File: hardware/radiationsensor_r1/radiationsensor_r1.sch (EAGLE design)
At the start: 37 parts, among them CN1 1X06, U1 LMP7721, U2 MAX4477, U4 MAX4477, U5 50k

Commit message: radiation sensor r1 layout nearly complete
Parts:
- removed C17: 0.1uF, openct:CAP0603
- added C16: 1uF, openct:CAP0603
- added R16: THERM, openct:RESISTOR0603
- added R17: 10k, openct:RESISTOR0603
- C14: value 10uF 16V -> 10uF 10V
- C15: value 0.1uF -> 0.1uF 50V
- C4: value 1uF -> 1uF 50V
- CN1: value 1X06 -> 1X09; device openct:1X06 -> openct:1X09
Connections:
- removed net N$15: C14.1
- removed net VLOGIC: C17.1, CN1.1, U5.VDD
- new net VTEMP: CN1.1, R16.2, R17.1
- net 5V: now also C14.1, C16.1, CN1.8, R17.2, U5.VDD; no longer CN1.5
- net COMP_OUT: now also CN1.6; no longer CN1.3
- net CS: now also CN1.2
- net GND: now also C16.2, CN1.7, R16.1; no longer C17.2, CN1.4
- net MOSI: now also CN1.4
- net SCLK: now also CN1.3
- net VBIAS: now also CN1.9; no longer CN1.6
- net VOUT: now also CN1.5; no longer CN1.2
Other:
- moved on the sheet: C14, C15, C4

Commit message: schematic and board cleanup
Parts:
- C1: value 0.01uF -> 0.01uF 50V
- C6: value 0.1uF -> 4.7uF
- R10, R11, R8, R9: value 100k -> 51k
- R12: value 51.k -> 3.3k
- R3: value 10M -> 47M
- R5, R7: value 20k -> 33k
- renumbered D2 to D1
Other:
- note added: "(STACK OF 4"
- note added: "(~1100X GAIN)"
- note added: "(~15mv HYSTERESIS)"
- note added: "BASED ON MAXIM APPLICATION NOTE 2236"
- note added: "DECOUPLING"
- note added: "PETER JANSEN, JUNE 2015"
- note added: "PHOTODIODES)"
- note added: "RADIATION SENSOR (REVISION 1)"
- note added: "TEMPERATURE SENSOR"
- moved on the sheet: C10, C13, C14, C15, C16, R14, R15, R16, R17, R8, R9, U5

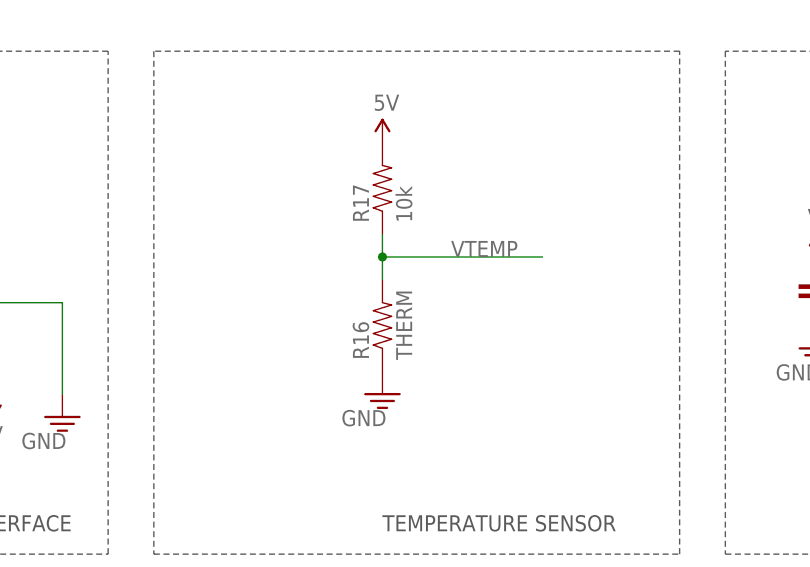
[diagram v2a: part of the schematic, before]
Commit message: Added part in library for radiation sensor rev1
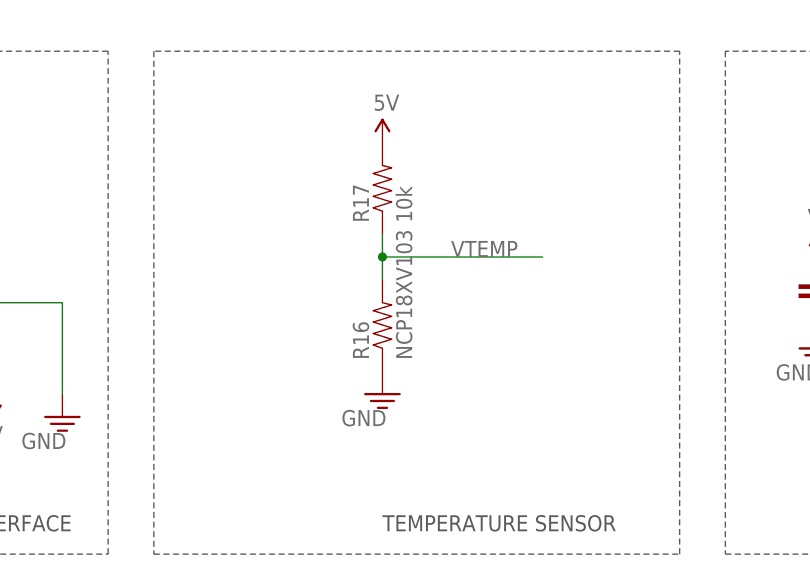
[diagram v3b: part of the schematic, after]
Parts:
- R16: value THERM -> NCP18XV103
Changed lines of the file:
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@@
 <part name="U$14" library="openct" deviceset="5V" device=""/>
 <part name="U$15" library="openct" deviceset="5V" device=""/>
-<part name="R16" library="openct" deviceset="RESISTOR" device="0603" value="THERM"/>
+<part name="R16" library="openct" deviceset="RESISTOR" device="0603" value="NCP18XV103"/>
 <part name="GND15" library="openct" deviceset="GND" device=""/>
 <part name="R17" library="openct" deviceset="RESISTOR" device="0603" value="10k"/>

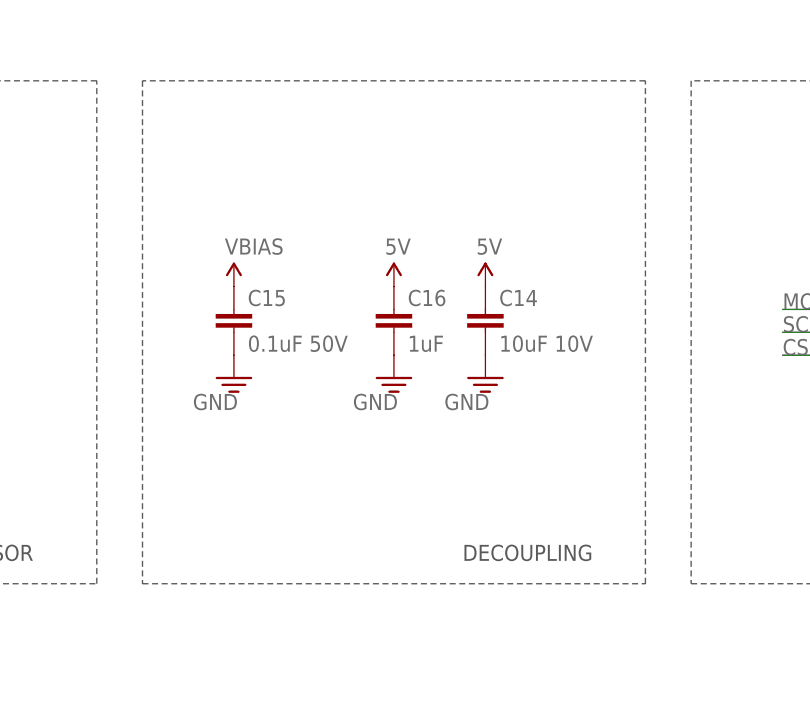
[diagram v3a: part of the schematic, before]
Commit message: Added shield connection to radiation sensor rev1
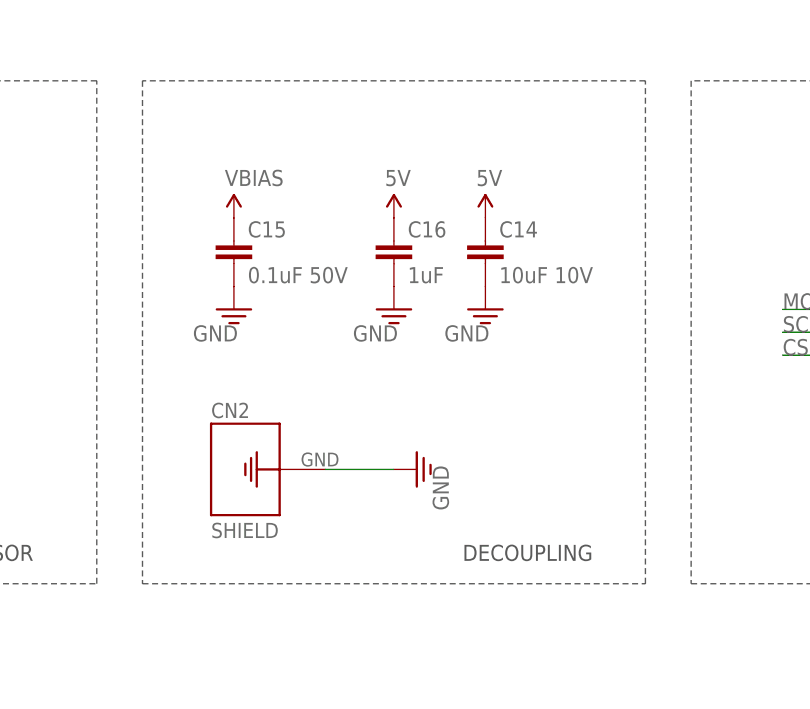
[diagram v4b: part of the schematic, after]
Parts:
- added CN2: GROUND-PAD, openct:GROUND-PAD
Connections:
- net GND: now also CN2.1
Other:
- moved on the sheet: C14, C15, C16
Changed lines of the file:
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@@
 <part name="U$6" library="openct" deviceset="5V" device=""/>
 <part name="GND16" library="openct" deviceset="GND" device=""/>
+<part name="CN2" library="openct" deviceset="GROUND-PAD" device=""/>
+<part name="GND18" library="openct" deviceset="GND" device=""/>
 </parts>
 <sheets>
@@
 <instance part="C13" gate="G$1" x="205.74" y="-66.04"/>
 <instance part="GND14" gate="1" x="205.74" y="-71.12"/>
-<instance part="C14" gate="G$1" x="119.38" y="-58.42"/>
-<instance part="GND19" gate="1" x="119.38" y="-63.5"/>
-<instance part="U$1" gate="G$1" x="91.44" y="-53.34"/>
-<instance part="C15" gate="G$1" x="91.44" y="-58.42"/>
-<instance part="GND20" gate="1" x="91.44" y="-63.5"/>
+<instance part="C14" gate="G$1" x="119.38" y="-50.8"/>
+<instance part="GND19" gate="1" x="119.38" y="-55.88"/>
+<instance part="U$1" gate="G$1" x="91.44" y="-45.72"/>
+<instance part="C15" gate="G$1" x="91.44" y="-50.8"/>
+<instance part="GND20" gate="1" x="91.44" y="-55.88"/>
 <instance part="D1" gate="G$1" x="-27.94" y="5.08" rot="R180"/>
 <instance part="U$14" gate="G$1" x="162.56" y="-48.26"/>
-<instance part="U$15" gate="G$1" x="119.38" y="-53.34"/>
+<instance part="U$15" gate="G$1" x="119.38" y="-45.72"/>
 <instance part="R16" gate="G$1" x="43.18" y="-60.96" rot="R90"/>
 <instance part="GND15" gate="1" x="43.18" y="-68.58"/>
@@
 <instance part="U$22" gate="G$1" x="0" y="-68.58" rot="R180"/>
 <instance part="U$23" gate="G$1" x="-7.62" y="-68.58" rot="R180"/>
-<instance part="C16" gate="G$1" x="109.22" y="-58.42"/>
-<instance part="U$6" gate="G$1" x="109.22" y="-53.34"/>
-<instance part="GND16" gate="1" x="109.22" y="-63.5"/>
+<instance part="C16" gate="G$1" x="109.22" y="-50.8"/>
+<instance part="U$6" gate="G$1" x="109.22" y="-45.72"/>
+<instance part="GND16" gate="1" x="109.22" y="-55.88"/>
+<instance part="CN2" gate="G$1" x="96.52" y="-73.66"/>
+<instance part="GND18" gate="1" x="111.76" y="-73.66" rot="R90"/>
 </instances>
 <busses>
@@
 <pinref part="GND16" gate="1" pin="GND"/>
 </segment>
-</net>
+<segment>
+<pinref part="CN2" gate="G$1" pin="1"/>
+<wire x1="101.6" y1="-73.66" x2="109.22" y2="-73.66" width="0.1524" layer="91"/>
+<pinref part="GND18" gate="1" pin="GND"/>
+</segment>
+</net>
